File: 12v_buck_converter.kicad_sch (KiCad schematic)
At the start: 23 parts, among them IC1 TPS56A37RPAR, Q4 BUK9K52-60RAX

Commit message: finished footprint assignment
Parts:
- Q4: footprint (none) -> Package_TO_SOT_SMD:LFPAK56
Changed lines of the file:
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@@
 			)
 		)
-		(property "Footprint" ""
+		(property "Footprint" "Package_TO_SOT_SMD:LFPAK56"
 			(at 208.28 91.44 0)
 			(effects
@@
 			)
 		)
-		(property "Footprint" ""
+		(property "Footprint" "Package_TO_SOT_SMD:LFPAK56"
 			(at 208.28 104.14 0)
 			(effects

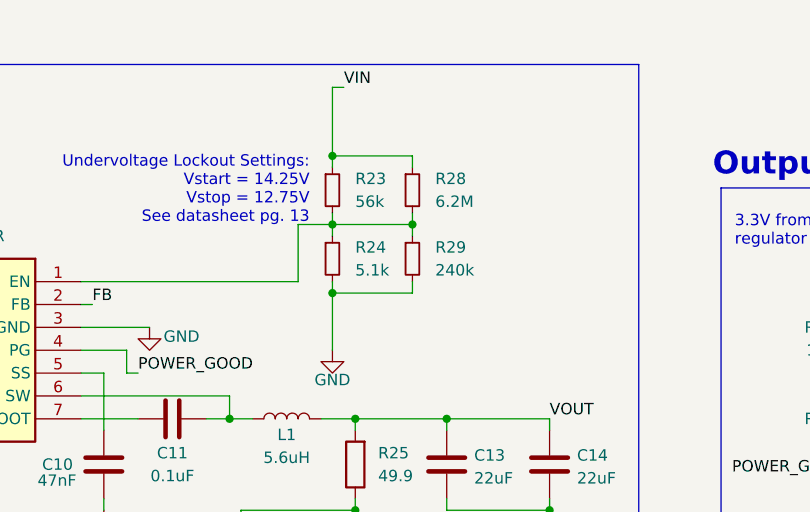
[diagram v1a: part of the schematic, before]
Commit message: removed parallel resistors
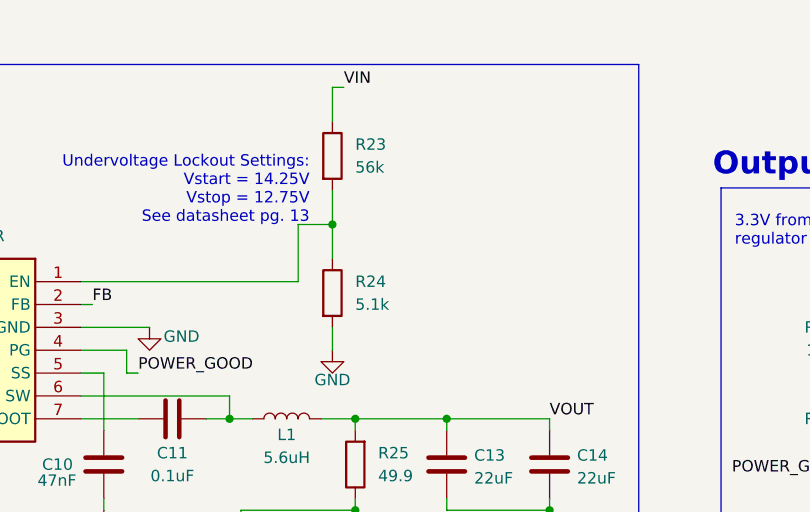
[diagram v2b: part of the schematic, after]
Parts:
- removed R28: 6.2M, Resistor_SMD:R_0805_2012Metric, symbol Device:R_Small
- removed R29: 240k, Resistor_SMD:R_0805_2012Metric, symbol Device:R_Small
- R23, R24: symbol Device:R_Small -> Device:R
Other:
- moved on the sheet: R23, R24

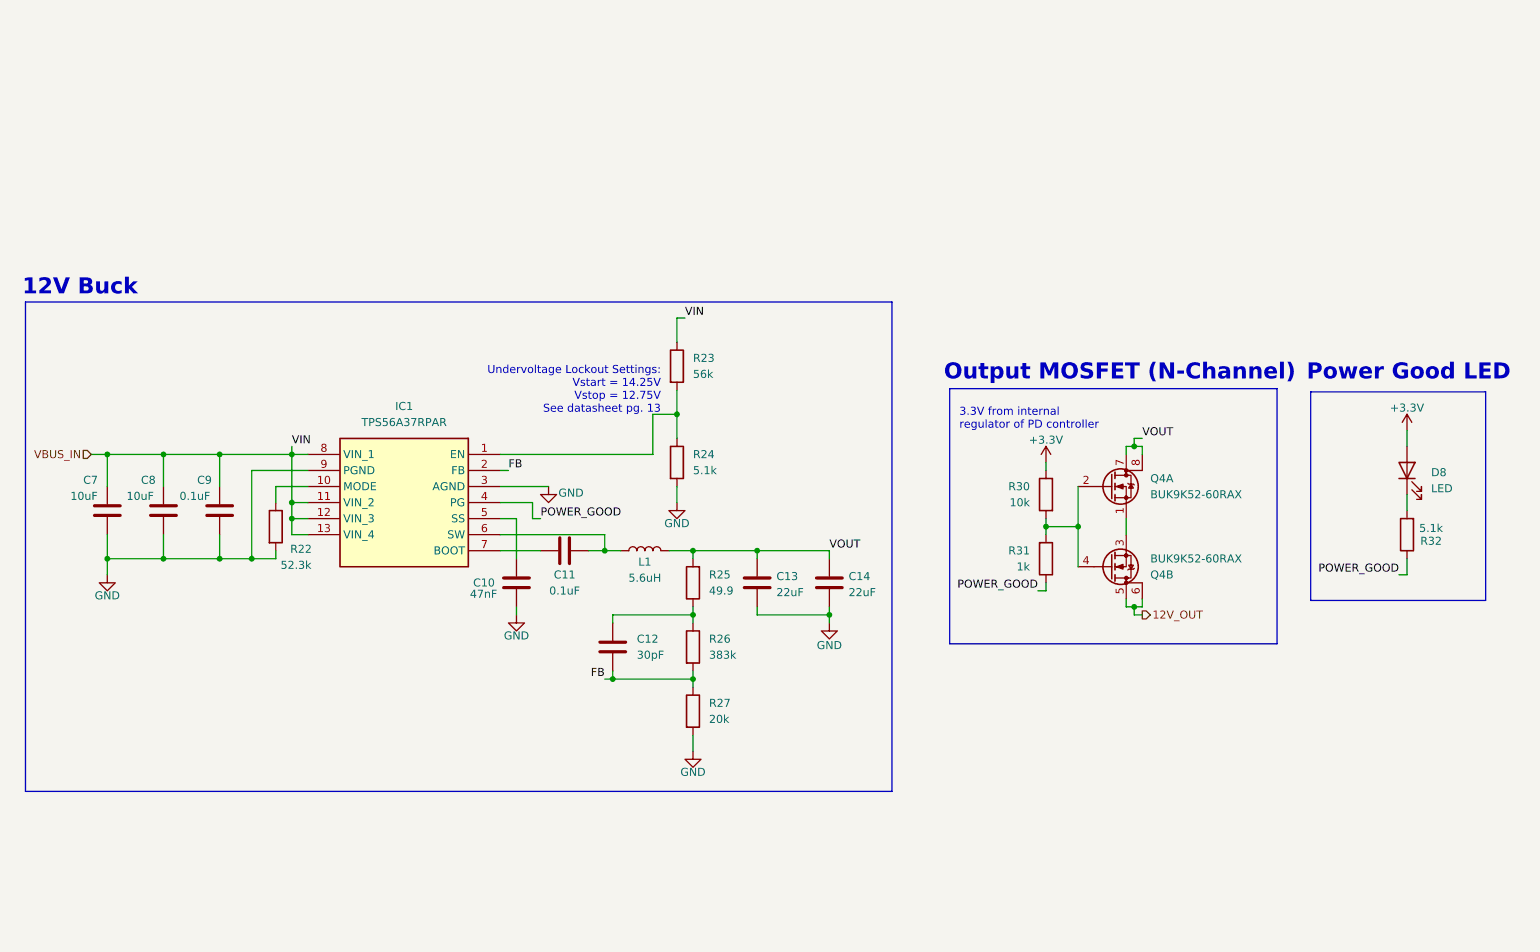
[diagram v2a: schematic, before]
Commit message: address review changes, add more output protections
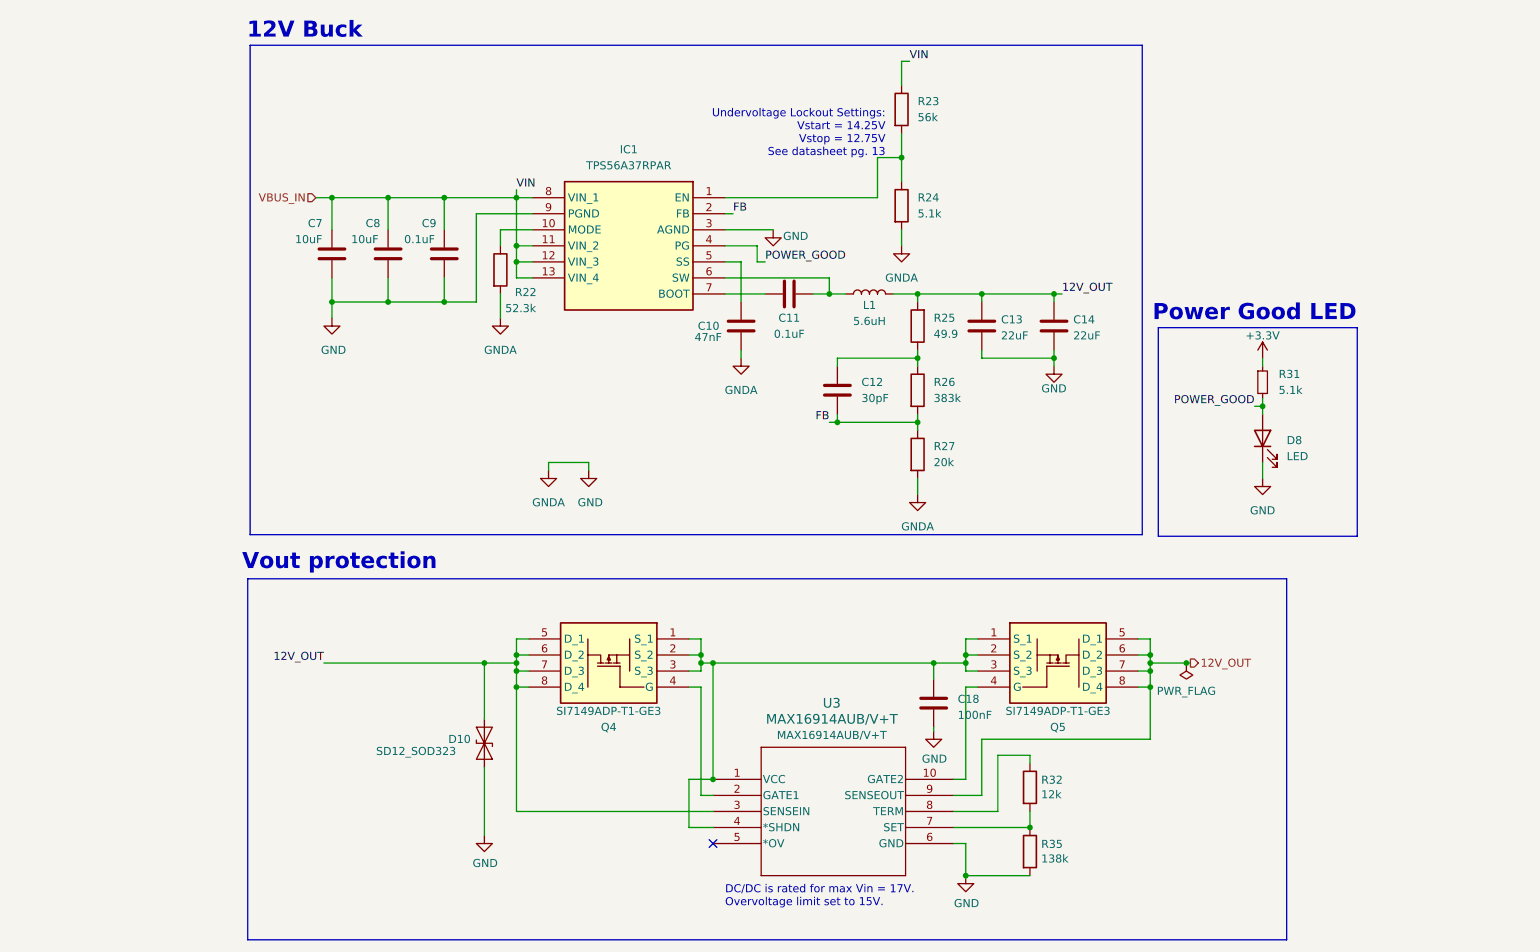
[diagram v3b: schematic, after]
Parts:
- removed Q4: BUK9K52-60RAX, Package_TO_SOT_SMD:LFPAK56, symbol Device:Q_Dual_NMOS_S1G1S2G2D2D2D1D1
- removed R30: 10k, Resistor_SMD:R_0805_2012Metric, symbol Device:R
- removed R31: 1k, Resistor_SMD:R_0805_2012Metric, symbol Device:R
- added C18: 100nF, Capacitor_SMD:C_0805_2012Metric, symbol Device:C
- added D10: SD12_SOD323, Diode_SMD:D_SOD-323, symbol Diode:SD12_SOD323
- added Q4, Q5: SI7149ADP-T1-GE3, UTSVT_ICs:POWERPAKSO-8, symbol utsvt-chips:SI7149ADP-T1-GE3
- added R31: 5.1k, symbol Device:R_Small
- added R35: 138k, Resistor_SMD:R_0805_2012Metric, symbol Device:R
- added U3: MAX16914AUB/V+T, UTSVT_ICs:21-0061L_MXM, symbol utsvt-chips:MAX16914AUB_V+T
- R32: value 5.1k -> 12k
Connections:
- net VOUT is gone; now on net 12V_OUT: C13.1, C14.1, L1.2, R25.2
- net +3.3V: now also R31.1; no longer D8.2 (A)
- net 12V_OUT: now also D10.2 (A2), Q4.5 (D_1), Q4.6 (D_2), Q4.7 (D_3), Q4.8 (D_4), Q5.5 (D_1), Q5.6 (D_2), Q5.7 (D_3), Q5.8 (D_4), U3.3 (SENSEIN), U3.9 (SENSEOUT)
- net GND: now also D8.1 (K), C18.2, D10.1 (A1), R35.2, U3.6 (GND)
- net POWER_GOOD: now also D8.2 (A), R31.2; no longer R32.1
- net at R32.2: now also R35.1, U3.7 (SET); no longer D8.1 (K)
- new net: R32.1, U3.8 (TERM)
- new net: C18.1, Q4.1 (S_1), Q4.2 (S_2), Q4.3 (S_3), Q5.1 (S_1), Q5.2 (S_2), Q5.3 (S_3), U3.1 (VCC), U3.4 (*SHDN)
- new net: Q4.4 (G), U3.2 (GATE1)
- new net: Q5.4 (G), U3.10 (GATE2)
- no-connect marks 0 -> 1
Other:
- note added: "DC/DC is rated for max Vin = 17V. Overvoltage limit set to 15V."
- note added: "Vout protection"
- note removed: "3.3V from internal regulator of PD controller"
- note removed: "Output MOSFET (N-Channel)"
- moved on the sheet: C10, C11, C12, C13, C14, C7, C8, C9, IC1, L1, R22, R23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

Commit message: footprint assignment again
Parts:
- R30: renamed from R31; footprint (none) -> Resistor_SMD:R_0805_2012Metric
- renumbered C9 to C10, C10 to C11, C11 to C12, C12 to C13, C18 to C14, C13 to C15, C14 to C16, C7 to C8, C8 to C9, D8 to D10, D10 to D9, R32 to R28, R35 to R29
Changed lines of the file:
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@@
 		(dnp no)
 		(fields_autoplaced yes)
-		(property "Reference" "#PWR030"
+		(property "Reference" "#PWR049"
 			(at 144.78 77.47 0)
 			(effects
@@
 			(project ""
 				(path "/f58400c5-df4b-4929-8d2b-33c0fe23fcd9/01d27e83-9627-42d8-8cf9-628e44513f14"
-					(reference "#PWR030")
+					(reference "#PWR049")
 					(unit 1)
 				)
@@
 		(on_board yes)
 		(dnp no)
-		(property "Reference" "C13"
+		(property "Reference" "C15"
 			(at 185.928 65.024 0)
 			(effects
@@
 			(project "USBCPowerPCB"
 				(path "/f58400c5-df4b-4929-8d2b-33c0fe23fcd9/01d27e83-9627-42d8-8cf9-628e44513f14"
-					(reference "C13")
+					(reference "C15")
 					(unit 1)
 				)
@@
 		(on_board yes)
 		(dnp no)
-		(property "Reference" "R32"
+		(property "Reference" "R28"
 			(at 192.278 137.8966 0)
 			(effects
@@
 			(project "USBCPowerPCB"
 				(path "/f58400c5-df4b-4929-8d2b-33c0fe23fcd9/01d27e83-9627-42d8-8cf9-628e44513f14"
-					(reference "R32")
+					(reference "R28")
 					(unit 1)
 				)
@@
 		(on_board yes)
 		(dnp no)
-		(property "Reference" "#PWR052"
+		(property "Reference" "#PWR048"
 			(at 120.65 95.25 0)
 			(effects
@@
 			(project "USBCPowerPCB"
 				(path "/f58400c5-df4b-4929-8d2b-33c0fe23fcd9/01d27e83-9627-42d8-8cf9-628e44513f14"
-					(reference "#PWR052")
+					(reference "#PWR048")
 					(unit 1)
 				)
@@
 		(dnp no)
 		(fields_autoplaced yes)
-		(property "Reference" "#PWR032"
+		(property "Reference" "#PWR051"
 			(at 170.18 59.69 0)
 			(effects
@@
 			(project ""
 				(path "/f58400c5-df4b-4929-8d2b-33c0fe23fcd9/01d27e83-9627-42d8-8cf9-628e44513f14"
-					(reference "#PWR032")
+					(reference "#PWR051")
 					(unit 1)
 				)
@@
 		(dnp no)
 		(fields_autoplaced yes)
-		(property "Reference" "C12"
+		(property "Reference" "C13"
 			(at 163.83 74.9299 0)
 			(effects
@@
 			(project "USBCPowerPCB"
 				(path "/f58400c5-df4b-4929-8d2b-33c0fe23fcd9/01d27e83-9627-42d8-8cf9-628e44513f14"
-					(reference "C12")
+					(reference "C13")
 					(unit 1)
 				)
@@
 		(on_board yes)
 		(dnp no)
-		(property "Reference" "C10"
+		(property "Reference" "C11"
 			(at 137.922 66.04 0)
 			(effects
@@
 			(project "USBCPowerPCB"
 				(path "/f58400c5-df4b-4929-8d2b-33c0fe23fcd9/01d27e83-9627-42d8-8cf9-628e44513f14"
-					(reference "C10")
+					(reference "C11")
 					(unit 1)
 				)
@@
 		(on_board yes)
 		(dnp no)
-		(property "Reference" "#PWR029"
+		(property "Reference" "#PWR044"
 			(at 80.01 71.12 0)
 			(effects
@@
 			(project "USBCPowerPCB"
 				(path "/f58400c5-df4b-4929-8d2b-33c0fe23fcd9/01d27e83-9627-42d8-8cf9-628e44513f14"
-					(reference "#PWR029")
+					(reference "#PWR044")
 					(unit 1)
 				)
@@
 		(dnp no)
 		(fields_autoplaced yes)
-		(property "Reference" "#PWR039"
+		(property "Reference" "#PWR046"
 			(at 106.68 71.12 0)
 			(effects
@@
 			(project ""
 				(path "/f58400c5-df4b-4929-8d2b-33c0fe23fcd9/01d27e83-9627-42d8-8cf9-628e44513f14"
-					(reference "#PWR039")
+					(reference "#PWR046")
 					(unit 1)
 				)
@@
 		(dnp no)
 		(fields_autoplaced yes)
-		(property "Reference" "#PWR040"
+		(property "Reference" "#PWR057"
 			(at 227.33 96.52 0)
 			(effects
@@
 			(project ""
 				(path "/f58400c5-df4b-4929-8d2b-33c0fe23fcd9/01d27e83-9627-42d8-8cf9-628e44513f14"
-					(reference "#PWR040")
+					(reference "#PWR057")
 					(unit 1)
 				)
@@
 		(on_board yes)
 		(dnp no)
-		(property "Reference" "#PWR063"
+		(property "Reference" "#PWR053"
 			(at 175.26 136.525 0)
 			(effects
@@
 			(project "USBCPowerPCB"
 				(path "/f58400c5-df4b-4929-8d2b-33c0fe23fcd9/01d27e83-9627-42d8-8cf9-628e44513f14"
-					(reference "#PWR063")
+					(reference "#PWR053")
 					(unit 1)
 				)
@@
 		(on_board yes)
 		(dnp no)
-		(property "Reference" "C11"
+		(property "Reference" "C12"
 			(at 152.4 64.77 90)
 			(effects
@@
 			(project "USBCPowerPCB"
 				(path "/f58400c5-df4b-4929-8d2b-33c0fe23fcd9/01d27e83-9627-42d8-8cf9-628e44513f14"
-					(reference "C11")
+					(reference "C12")
 					(unit 1)
 				)
@@
 		(on_board yes)
 		(dnp no)
-		(property "Reference" "#PWR034"
+		(property "Reference" "#PWR055"
 			(at 194.31 78.74 0)
 			(effects
@@
 			(project "USBCPowerPCB"
 				(path "/f58400c5-df4b-4929-8d2b-33c0fe23fcd9/01d27e83-9627-42d8-8cf9-628e44513f14"
-					(reference "#PWR034")
+					(reference "#PWR055")
 					(unit 1)
 				)
@@
 		(on_board yes)
 		(dnp no)
-		(property "Reference" "C14"
+		(property "Reference" "C16"
 			(at 197.358 65.024 0)
 			(effects
@@
 			(project "USBCPowerPCB"
 				(path "/f58400c5-df4b-4929-8d2b-33c0fe23fcd9/01d27e83-9627-42d8-8cf9-628e44513f14"
-					(reference "C14")
+					(reference "C16")
 					(unit 1)
 				)
@@
 		(on_board yes)
 		(dnp no)
-		(property "Reference" "R35"
+		(property "Reference" "R29"
 			(at 192.278 148.0566 0)
 			(effects
@@
 			(project "USBCPowerPCB"
 				(path "/f58400c5-df4b-4929-8d2b-33c0fe23fcd9/01d27e83-9627-42d8-8cf9-628e44513f14"
-					(reference "R35")
+					(reference "R29")
 					(unit 1)
 				)
@@
 		(on_board yes)
 		(dnp no)
-		(property "Reference" "#PWR036"
+		(property "Reference" "#PWR056"
 			(at 227.33 74.93 0)
 			(effects
@@
 			(project ""
 				(path "/f58400c5-df4b-4929-8d2b-33c0fe23fcd9/01d27e83-9627-42d8-8cf9-628e44513f14"
-					(reference "#PWR036")
+					(reference "#PWR056")
 					(unit 1)
 				)
@@
 		(dnp no)
 		(fields_autoplaced yes)
-		(property "Reference" "C18"
+		(property "Reference" "C14"
 			(at 179.07 125.095 0)
 			(effects
@@
 			(project "USBCPowerPCB"
 				(path "/f58400c5-df4b-4929-8d2b-33c0fe23fcd9/01d27e83-9627-42d8-8cf9-628e44513f14"
-					(reference "C18")
+					(reference "C14")
 					(unit 1)
 				)
@@
 		(dnp no)
 		(fields_autoplaced yes)
-		(property "Reference" "#PWR033"
+		(property "Reference" "#PWR052"
 			(at 172.72 99.06 0)
 			(effects
@@
 			(project "USBCPowerPCB"
 				(path "/f58400c5-df4b-4929-8d2b-33c0fe23fcd9/01d27e83-9627-42d8-8cf9-628e44513f14"
-					(reference "#PWR033")
+					(reference "#PWR052")
 					(unit 1)
 				)
@@
 		(on_board yes)
 		(dnp no)
-		(property "Reference" "C8"
+		(property "Reference" "C9"
 			(at 85.344 49.784 0)
 			(effects
@@
 			(project "USBCPowerPCB"
 				(path "/f58400c5-df4b-4929-8d2b-33c0fe23fcd9/01d27e83-9627-42d8-8cf9-628e44513f14"
-					(reference "C8")
+					(reference "C9")
 					(unit 1)
 				)
@@
 		(dnp no)
 		(fields_autoplaced yes)
-		(property "Reference" "D8"
+		(property "Reference" "D10"
 			(at 231.14 84.1374 90)
 			(effects
@@
 			(project "USBCPowerPCB"
 				(path "/f58400c5-df4b-4929-8d2b-33c0fe23fcd9/01d27e83-9627-42d8-8cf9-628e44513f14"
-					(reference "D8")
+					(reference "D10")
 					(unit 1)
 				)
@@
 		(on_board yes)
 		(dnp no)
-		(property "Reference" "#PWR064"
+		(property "Reference" "#PWR054"
 			(at 180.34 159.385 0)
 			(effects
@@
 			(project "USBCPowerPCB"
 				(path "/f58400c5-df4b-4929-8d2b-33c0fe23fcd9/01d27e83-9627-42d8-8cf9-628e44513f14"
-					(reference "#PWR064")
+					(reference "#PWR054")
 					(unit 1)
 				)
@@
 		(on_board yes)
 		(dnp no)
-		(property "Reference" "C7"
+		(property "Reference" "C8"
 			(at 76.2 49.784 0)
 			(effects
@@
 			(project "USBCPowerPCB"
 				(path "/f58400c5-df4b-4929-8d2b-33c0fe23fcd9/01d27e83-9627-42d8-8cf9-628e44513f14"
-					(reference "C7")
+					(reference "C8")
 					(unit 1)
 				)
@@
 		(dnp no)
 		(fields_autoplaced yes)
-		(property "Reference" "#PWR051"
+		(property "Reference" "#PWR047"
 			(at 114.3 95.25 0)
 			(effects
@@
 			(project "USBCPowerPCB"
 				(path "/f58400c5-df4b-4929-8d2b-33c0fe23fcd9/01d27e83-9627-42d8-8cf9-628e44513f14"
-					(reference "#PWR051")
+					(reference "#PWR047")
 					(unit 1)
 				)
@@
 		(on_board yes)
 		(dnp no)
-		(property "Reference" "C9"
+		(property "Reference" "C10"
 			(at 94.234 49.784 0)
 			(effects
@@
 			(project "USBCPowerPCB"
 				(path "/f58400c5-df4b-4929-8d2b-33c0fe23fcd9/01d27e83-9627-42d8-8cf9-628e44513f14"
-					(reference "C9")
+					(reference "C10")
 					(unit 1)
 				)
@@
 		(dnp no)
 		(fields_autoplaced yes)
-		(property "Reference" "#FLG03"
+		(property "Reference" "#FLG01"
 			(at 215.265 121.285 0)
 			(effects
@@
 			(project "USBCPowerPCB"
 				(path "/f58400c5-df4b-4929-8d2b-33c0fe23fcd9/01d27e83-9627-42d8-8cf9-628e44513f14"
-					(reference "#FLG03")
+					(reference "#FLG01")
 					(unit 1)
 				)
@@
 		(on_board yes)
 		(dnp no)
-		(property "Reference" "D10"
+		(property "Reference" "D9"
 			(at 98.425 131.445 90)
 			(effects
@@
 			(project "USBCPowerPCB"
 				(path "/f58400c5-df4b-4929-8d2b-33c0fe23fcd9/01d27e83-9627-42d8-8cf9-628e44513f14"
-					(reference "D10")
+					(reference "D9")
 					(unit 1)
 				)
@@
 		(dnp no)
 		(fields_autoplaced yes)
-		(property "Reference" "R31"
+		(property "Reference" "R30"
 			(at 229.87 73.6599 0)
 			(effects
@@
 			)
 		)
-		(property "Footprint" ""
+		(property "Footprint" "Resistor_SMD:R_0805_2012Metric"
 			(at 227.33 74.93 0)
 			(effects
@@
 			(project ""
 				(path "/f58400c5-df4b-4929-8d2b-33c0fe23fcd9/01d27e83-9627-42d8-8cf9-628e44513f14"
-					(reference "R31")
+					(reference "R30")
 					(unit 1)
 				)
@@
 		(on_board yes)
 		(dnp no)
-		(property "Reference" "#PWR031"
+		(property "Reference" "#PWR050"
 			(at 149.86 57.15 0)
 			(effects
@@
 			(project "USBCPowerPCB"
 				(path "/f58400c5-df4b-4929-8d2b-33c0fe23fcd9/01d27e83-9627-42d8-8cf9-628e44513f14"
-					(reference "#PWR031")
+					(reference "#PWR050")
 					(unit 1)
 				)
@@
 		(on_board yes)
 		(dnp no)
-		(property "Reference" "#PWR062"
+		(property "Reference" "#PWR045"
 			(at 104.14 153.035 0)
 			(effects
@@
 			(project "USBCPowerPCB"
 				(path "/f58400c5-df4b-4929-8d2b-33c0fe23fcd9/01d27e83-9627-42d8-8cf9-628e44513f14"
-					(reference "#PWR062")
-					(unit 1)
-				)
+					(reference "#PWR045")
+					(unit 1)
+				)
